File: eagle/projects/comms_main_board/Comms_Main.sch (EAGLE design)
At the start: 159 parts, among them J1 WRL-00593, J10 MOL-KK-2-RA, J11 MOL-KK-3P-RA, J12 MOL-KK-3P-RA, J13 MOL-KK-3P-RA, J14 MOL-KK-3P-RA, J15 MOL-KK-2-RA, J16 MOLKK_POW_2_RA, J17 MOLKK_POW_2_RA, J18 MOLKK_POW_2_RA, J19 MOLKK_POW_2_RA, J2 PRT-12639, J20 MOL-KK-2-RA, J3 PRT-12639, J4 PRT-12639, J5 PRT-12639, J6 MOL-KK-3P-RA, J7 MOL-KK-5P-V, J8 RECEPTACLE-2x20-254MM, J9 MOL-KK-3P-RA, Q1 CSD17579Q3A, U1 TPS562209DDCT, U10 MCP4541-103E/MS, U11 TPS562209DDCT, U12 MMBT3904-7-F, U13 MAX3232CSE+, U14 MAX4311, U2 LP2985-33DBVR, U3 LP5900TLX-3.3/NOPB, U4 TPS562209DDCT, U5 LMZ34002RKGR, U6 LM3488MMX/NOPB, U7 PCT2075D,118, U8 MS560702BA03-50, U9 MAX-M8Q

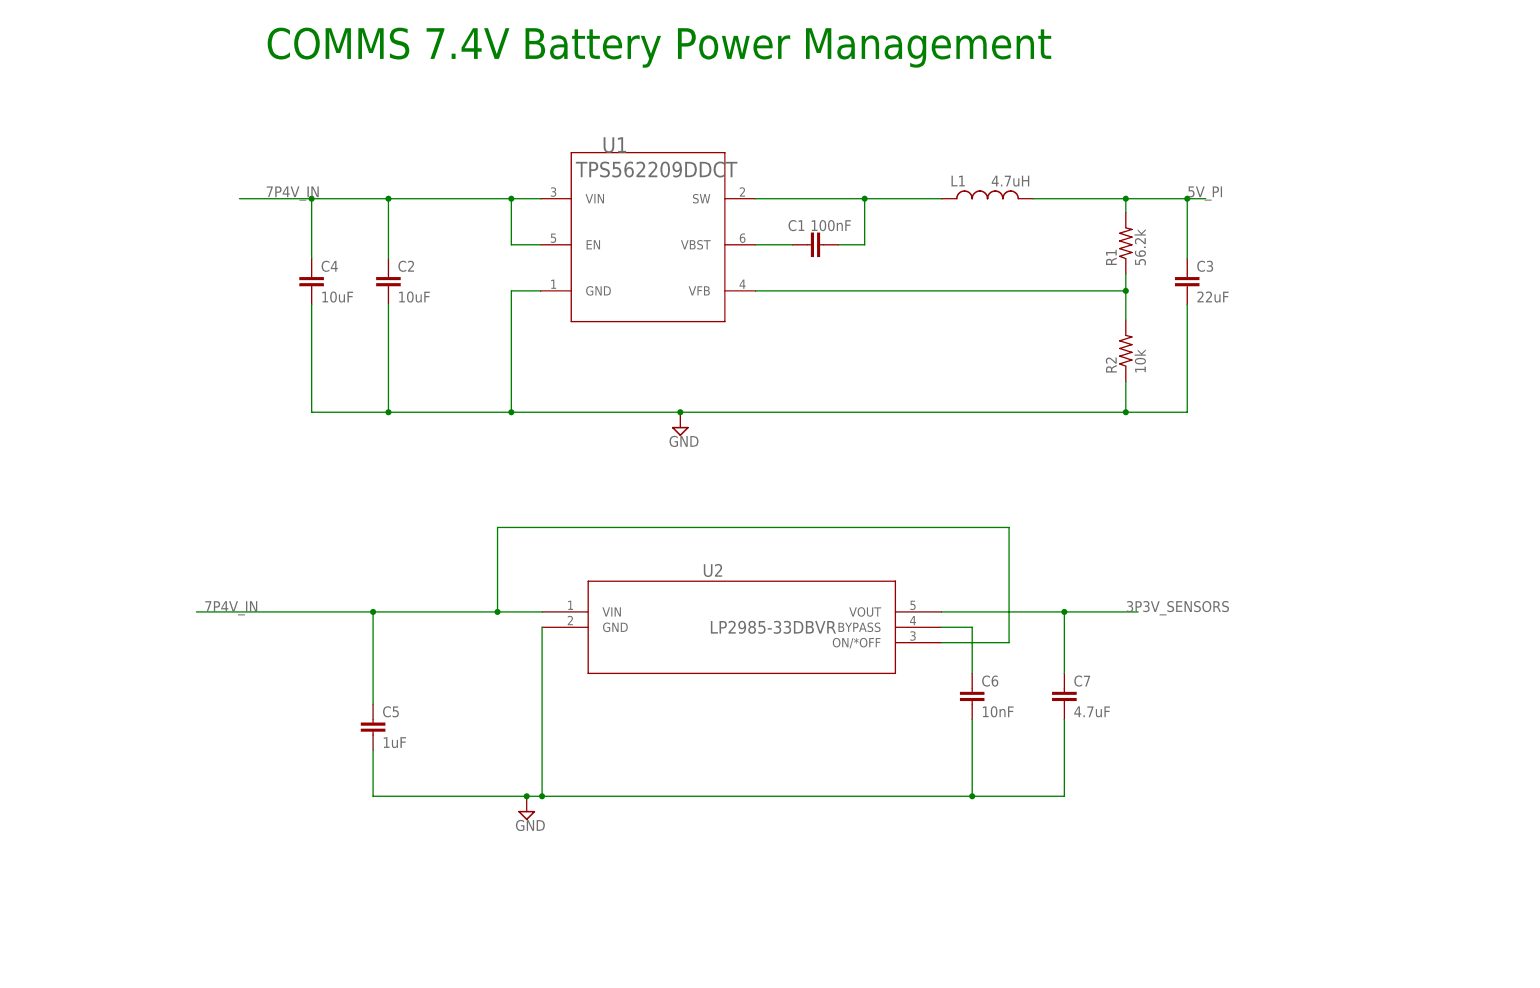
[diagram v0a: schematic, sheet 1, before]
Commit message: Added HW watchdog timer for pi. Changed KK connectors to SL and Mini-fit JR. Exported BOM. ERC passed.
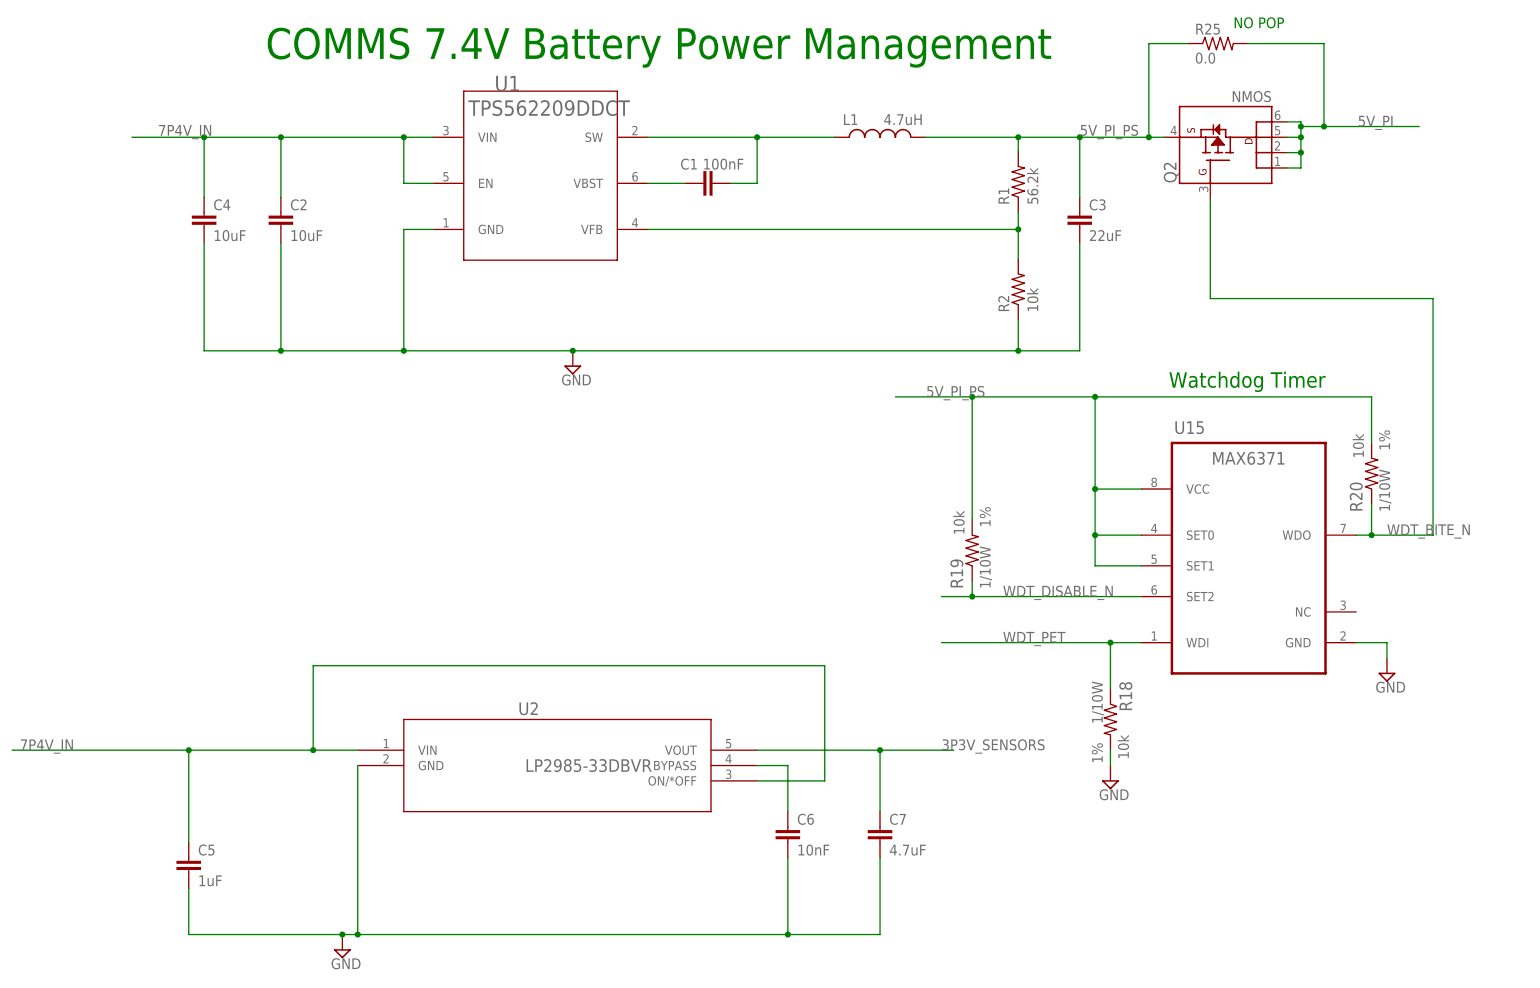
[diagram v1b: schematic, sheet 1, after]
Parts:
- removed TP21, TP22: TPTP15R, comms:TPTP15R
- added Q2: NMOS, comms:NMOS-1G-1S-4D_NMOS-6P_TSOP-6
- added R18, R19, R20: 10k, daqcs:RES_10R0_0603
- added R25: 0.0, comms:RES_0R0_0805
- added U15: MAX6371, daqcs:MAX63XX71KA_SOT23
- J10, J15, J20: value MOL-KK-2-RA -> MOL-SL-2-RA; device daqcs:MOLKK_2PIN_2RA_2RA -> comms:MOLSL_2PIN_SL2RA_RA
- J11, J12, J13, J14, J6, J9: value MOL-KK-3P-RA -> MOL-SL-3-RA; device daqcs:MOLKK_3PIN_3RA_RA -> comms:MOLSL_3PIN_SL3RA_RA
- J16, J17, J18, J19: value MOLKK_POW_2_RA -> MOL-MINIJR-2P-RA; device comms:MOLKK_POW_2PIN -> comms:39-30-02
- J7: value MOL-KK-5P-V -> MOL-SL-5-RA; device daqcs:MOLKK_5PIN_5RA_RA -> comms:MOLSL_5PIN_SL4RA_RA
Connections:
- removed net PI_GPIO5: J8.29, TP22.TP
- removed net PI_GPIO6: J8.31, TP21.TP
- new net 5V_PI_PS: C3.1, L1.2, Q2.S, R1.2, R19.2, R20.2, R25.1, U15.SET0, U15.SET1, U15.VCC
- new net WDT_BITE_N: Q2.G, R20.1, U15.WDO
- new net WDT_DISABLE_N: J8.29, R19.1, U15.SET2
- new net WDT_PET: J8.31, R18.1, U15.WDI
- net 5V_PI: now also Q2.D@1, Q2.D@2, Q2.D@3, Q2.D@4, R25.2; no longer C3.1, L1.2, R1.2
- net GND: now also R18.2, U15.GND
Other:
- note added: "NO POP"
- note added: "Watchdog Timer"
- moved on the sheet: C1, C2, C3, C4, C5, C6, C7, J16, J17, J18, J19, J6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

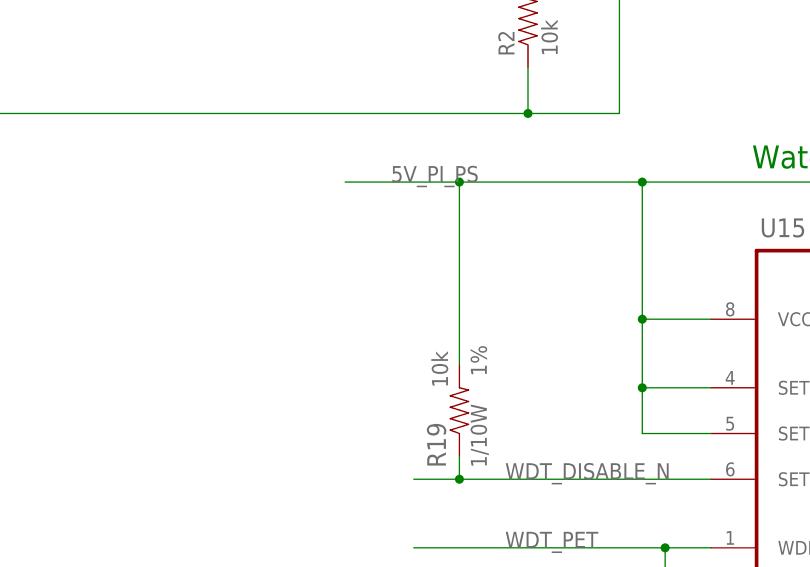
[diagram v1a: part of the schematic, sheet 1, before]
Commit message: Fixed MAX4311 footprint
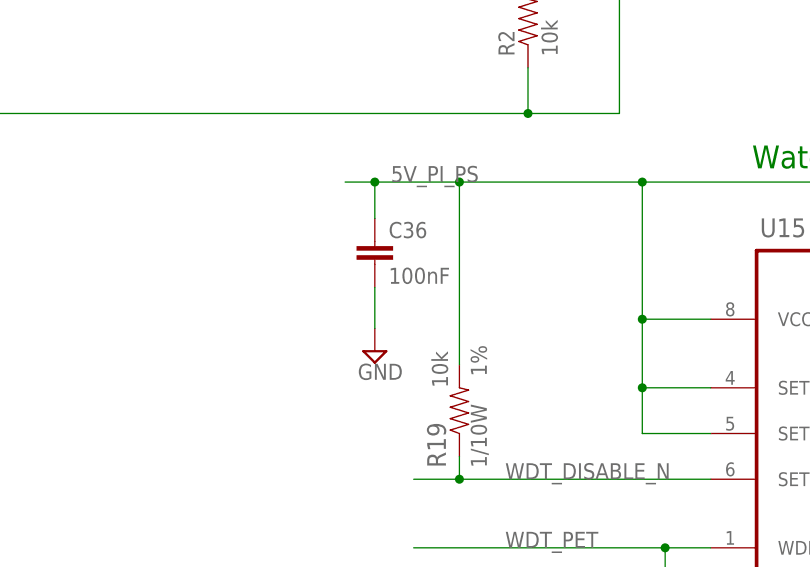
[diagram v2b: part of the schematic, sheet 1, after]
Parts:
- added C36: 100nF, comms:CAP_100NF0_0603
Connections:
- net 5V_PI_PS: now also C36.1
- net GND: now also C36.2
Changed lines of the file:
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@@
 <part name="J19" library="comms" deviceset="39-30-?02?" device="" value="MOL-MINIJR-2P-RA"/>
 <part name="J16" library="comms" deviceset="39-30-?02?" device="" value="MOL-MINIJR-2P-RA"/>
+<part name="C36" library="comms" deviceset="CAP" device="_0603" technology="_100NF0" value="100nF"/>
+<part name="SUPPLY33" library="supply2" deviceset="GND" device=""/>
 </parts>
 <sheets>
@@
 <instance part="Q2" gate="G$1" x="250.19" y="215.646" rot="R90"/>
 <instance part="R25" gate="G$1" x="248.92" y="231.14"/>
+<instance part="C36" gate="G$1" x="198.882" y="163.576"/>
+<instance part="SUPPLY33" gate="GND" x="198.882" y="153.924"/>
 </instances>
 <busses>
@@
 <pinref part="U15" gate="G$1" pin="GND"/>
 <wire x1="271.78" y1="132.08" x2="276.86" y2="132.08" width="0.1524" layer="91"/>
+</segment>
+<segment>
+<pinref part="SUPPLY33" gate="GND" pin="GND"/>
+<pinref part="C36" gate="G$1" pin="2"/>
+<wire x1="198.882" y1="156.464" x2="198.882" y2="161.036" width="0.1524" layer="91"/>
 </segment>
 </net>
@@
 </segment>
 <segment>
-<wire x1="195.58" y1="172.72" x2="208.28" y2="172.72" width="0.1524" layer="91"/>
+<wire x1="195.58" y1="172.72" x2="198.882" y2="172.72" width="0.1524" layer="91"/>
+<wire x1="198.882" y1="172.72" x2="208.28" y2="172.72" width="0.1524" layer="91"/>
 <wire x1="208.28" y1="172.72" x2="228.6" y2="172.72" width="0.1524" layer="91"/>
 <wire x1="228.6" y1="172.72" x2="274.32" y2="172.72" width="0.1524" layer="91"/>
@@
 <pinref part="R20" gate="G$1" pin="2"/>
 <wire x1="274.32" y1="165.1" x2="274.32" y2="172.72" width="0.1524" layer="91"/>
-</segment>
-</net>
+<pinref part="C36" gate="G$1" pin="1"/>
+<wire x1="198.882" y1="168.656" x2="198.882" y2="172.72" width="0.1524" layer="91"/>
+<junction x="198.882" y="172.72"/>
+</segment>
+</net>

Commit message: Added 2x2 connector for Pi RUN pin and modified schematic for H/W WDT to drive that pin
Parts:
- removed Q2: NMOS, comms:NMOS-1G-1S-4D_NMOS-6P_TSOP-6
- removed R25: 0.0, comms:RES_0R0_0805
- added J21: RECEPTACLE-2x2-254MM, comms:RECEPTACLE-2X2-254MM
- added TP21: TPTP15R, comms:TPTP15R
- R19: value 10k -> 0; device daqcs:RES_10R0_0603 -> comms:RES_0R0_0603
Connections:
- removed net 5V_PI_PS: C3.1, C36.1, L1.2, Q2.S, R1.2, R19.2, R20.2, R25.1, U15.SET0, U15.SET1, U15.VCC
- removed net WDT_DISABLE_N: J8.29, R19.1, U15.SET2
- new net N$59: R19.2, U15.SET2
- new net PI_GPIO5: J8.29, TP21.TP
- net 5V_PI: now also C3.1, C36.1, L1.2, R1.2, R19.1, R20.2, U15.SET0, U15.SET1, U15.VCC; no longer Q2.D@1, Q2.D@2, Q2.D@3, Q2.D@4, R25.2
- net GND: now also J21.2
- net WDT_BITE_N: now also J21.4; no longer Q2.G
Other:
- note added: "PI Run pin pulled high"
- note added: "Pi Zero Run Pin Connector"
- moved on the sheet: J20, R19
